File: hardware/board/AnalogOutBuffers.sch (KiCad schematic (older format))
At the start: 19 parts, among them U10 OPA4197

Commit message: Re-do the motherboard
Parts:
- added C15: 0.1uF, Capacitor_SMD:C_0603_1608Metric_Pad1.08x0.95mm_HandSolder, symbol Device:C_Small
- added R36: 1k, Resistor_SMD:R_0603_1608Metric_Pad0.98x0.95mm_HandSolder, symbol Device:R_US
- added U2: LM4040-10, Package_TO_SOT_SMD:SOT-23, symbol winterbloom:LM4040-10
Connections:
- net -12V: now also R36.1
- net GND: now also C15.1, U2.1 (K)
- net -10V renamed -10v_DAC
- net -10v_DAC: now also C15.2, R36.2, U2.2 (A)
- net DAC_IN_1 renamed DAC_1_PRE
- net DAC_IN_2 renamed DAC_2_PRE
- net DAC_IN_3 renamed DAC_3_PRE
- net DAC_IN_4 renamed DAC_4_PRE
- net DAC_OUT_1 renamed DAC_3_POST
- net DAC_OUT_2 renamed DAC_4_POST
- net DAC_OUT_3 renamed DAC_1_POST
- net DAC_OUT_4 renamed DAC_2_POST
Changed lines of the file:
@@
 $Descr A4 11693 8268
 encoding utf-8
-Sheet 5 7
-Title ""
-Date ""
-Rev ""
-Comp ""
-Comment1 ""
-Comment2 ""
+Sheet 4 7
+Title "TestKit Motherboard"
+Date "2021-10-22"
+Rev "v1"
+Comp "Winterbloom"
+Comment1 "Alethea Flowers"
+Comment2 "CERN-OHL-P V2"
 Comment3 ""
 Comment4 ""
@@
 Wire Wire Line
 	1625 1400 1675 1400
-$Comp
-L power:-10V #PWR068
-U 1 1 60917606
-P 1150 1950
-F 0 "#PWR068" H 1150 2050 50  0001 C CNN
-F 1 "-10V" V 1150 2175 50  0000 C CNN
-F 2 "" H 1150 1950 50  0001 C CNN
-F 3 "" H 1150 1950 50  0001 C CNN
-	1    1150 1950
-	0    -1   -1   0
-$EndComp
 Wire Wire Line
 	2575 1500 2575 1950
@@
 Wire Wire Line
 	1650 2400 1700 2400
-$Comp
-L power:-10V #PWR069
-U 1 1 60917658
-P 1175 2950
-F 0 "#PWR069" H 1175 3050 50  0001 C CNN
-F 1 "-10V" V 1175 3175 50  0000 C CNN
-F 2 "" H 1175 2950 50  0001 C CNN
-F 3 "" H 1175 2950 50  0001 C CNN
-	1    1175 2950
-	0    -1   -1   0
-$EndComp
 Wire Wire Line
 	2600 2500 2600 2950
@@
 Wire Wire Line
 	1650 3375 1700 3375
-$Comp
-L power:-10V #PWR070
-U 1 1 60917690
-P 1175 3925
-F 0 "#PWR070" H 1175 4025 50  0001 C CNN
-F 1 "-10V" V 1175 4150 50  0000 C CNN
-F 2 "" H 1175 3925 50  0001 C CNN
-F 3 "" H 1175 3925 50  0001 C CNN
-	1    1175 3925
-	0    -1   -1   0
-$EndComp
 Wire Wire Line
 	2600 3475 2600 3925
@@
 Wire Wire Line
 	1650 4350 1700 4350
-$Comp
-L power:-10V #PWR071
-U 1 1 609176C8
-P 1175 4900
-F 0 "#PWR071" H 1175 5000 50  0001 C CNN
-F 1 "-10V" V 1175 5125 50  0000 C CNN
-F 2 "" H 1175 4900 50  0001 C CNN
-F 3 "" H 1175 4900 50  0001 C CNN
-	1    1175 4900
-	0    -1   -1   0
-$EndComp
 Wire Wire Line
 	2600 4450 2600 4900
@@
 0 - 2.5v
 Text HLabel 1175 2600 0    50   Input ~ 0
-DAC_IN_2
+DAC_2_PRE
 Text HLabel 1175 3575 0    50   Input ~ 0
-DAC_IN_3
+DAC_3_PRE
 Text HLabel 2600 3475 2    50   Input ~ 0
-DAC_OUT_1
+DAC_3_POST
 Text HLabel 2600 4450 2    50   Input ~ 0
-DAC_OUT_2
+DAC_4_POST
 Text HLabel 2575 1500 2    50   Input ~ 0
-DAC_OUT_3
+DAC_1_POST
 Text HLabel 2600 2500 2    50   Input ~ 0
-DAC_OUT_4
+DAC_2_POST
 $Comp
 L winterbloom:OPA4197 U10
@@
 $EndComp
 Text HLabel 1175 4550 0    50   Input ~ 0
-DAC_IN_4
+DAC_4_PRE
 Text HLabel 1150 1600 0    50   Input ~ 0
-DAC_IN_1
+DAC_1_PRE
+$Comp
+L winterbloom:LM4040-10 U?
+U 1 1 617993BE
+P 5075 3375
+AR Path="/60711259/617993BE" Ref="U?"  Part="1"
+AR Path="/61059808/617993BE" Ref="U?"  Part="1"
+AR Path="/608FFE97/617993BE" Ref="U2"  Part="1"
+F 0 "U2" V 5029 3454 50  0000 L CNN
+F 1 "LM4040-10" V 5120 3454 50  0000 L CNN
+F 2 "Package_TO_SOT_SMD:SOT-23" H 5075 3175 50  0001 C CIN
+F 3 "http://www.ti.com/lit/ds/symlink/lm4040-n.pdf" H 5075 3375 50  0001 C CIN
+F 4 "LM4040DIM3-10.0/NOPB" H 5075 3575 50  0001 C CNN "mpn"
+	1    5075 3375
+	0    1    1    0
+$EndComp
+$Comp
+L Device:R_US R?
+U 1 1 617993C4
+P 5075 3075
+AR Path="/60711259/617993C4" Ref="R?"  Part="1"
+AR Path="/61059808/617993C4" Ref="R?"  Part="1"
+AR Path="/608FFE97/617993C4" Ref="R36"  Part="1"
+F 0 "R36" H 5143 3121 50  0000 L CNN
+F 1 "1k" H 5143 3030 50  0000 L CNN
+F 2 "Resistor_SMD:R_0603_1608Metric_Pad0.98x0.95mm_HandSolder" V 5115 3065 50  0001 C CNN
+F 3 "~" H 5075 3075 50  0001 C CNN
+	1    5075 3075
+	1    0    0    -1
+$EndComp
+$Comp
+L power:GND #PWR?
+U 1 1 617993CA
+P 5075 3525
+AR Path="/60711259/617993CA" Ref="#PWR?"  Part="1"
+AR Path="/61059808/617993CA" Ref="#PWR?"  Part="1"
+AR Path="/608FFE97/617993CA" Ref="#PWR0159"  Part="1"
+F 0 "#PWR0159" H 5075 3275 50  0001 C CNN
+F 1 "GND" H 5150 3375 50  0000 R CNN
+F 2 "" H 5075 3525 50  0001 C CNN
+F 3 "" H 5075 3525 50  0001 C CNN
+	1    5075 3525
+	1    0    0    -1
+$EndComp
+$Comp
+L power:-12V #PWR?
+U 1 1 617993D0
+P 5075 2925
+AR Path="/60711259/617993D0" Ref="#PWR?"  Part="1"
+AR Path="/61059808/617993D0" Ref="#PWR?"  Part="1"
+AR Path="/608FFE97/617993D0" Ref="#PWR0160"  Part="1"
+F 0 "#PWR0160" H 5075 3025 50  0001 C CNN
+F 1 "-12V" H 4975 3075 50  0000 L CNN
+F 2 "" H 5075 2925 50  0001 C CNN
+F 3 "" H 5075 2925 50  0001 C CNN
+	1    5075 2925
+	1    0    0    -1
+$EndComp
+$Comp
+L Device:C_Small C?
+U 1 1 617993D6
+P 4825 3375
+AR Path="/60711259/617993D6" Ref="C?"  Part="1"
+AR Path="/61059808/617993D6" Ref="C?"  Part="1"
+AR Path="/608FFE97/617993D6" Ref="C15"  Part="1"
+F 0 "C15" H 5000 3350 50  0000 R CNN
+F 1 "0.1uF" H 5125 3425 50  0000 R CNN
+F 2 "Capacitor_SMD:C_0603_1608Metric_Pad1.08x0.95mm_HandSolder" H 4825 3375 50  0001 C CNN
+F 3 "~" H 4825 3375 50  0001 C CNN
+	1    4825 3375
+	-1   0    0    1
+$EndComp
+Wire Wire Line
+	4825 3275 4825 3225
+Wire Wire Line
+	4825 3225 5075 3225
+Connection ~ 5075 3225
+Wire Wire Line
+	4825 3475 4825 3525
+Wire Wire Line
+	4825 3525 5075 3525
+Connection ~ 5075 3525
+Text Label 5275 3225 0    50   ~ 0
+-10v_DAC
+Wire Wire Line
+	5275 3225 5075 3225
+Text Label 1150 1950 2    50   ~ 0
+-10v_DAC
+Text Label 1175 2950 2    50   ~ 0
+-10v_DAC
+Text Label 1175 3925 2    50   ~ 0
+-10v_DAC
+Text Label 1175 4900 2    50   ~ 0
+-10v_DAC
 $EndSCHEMATC

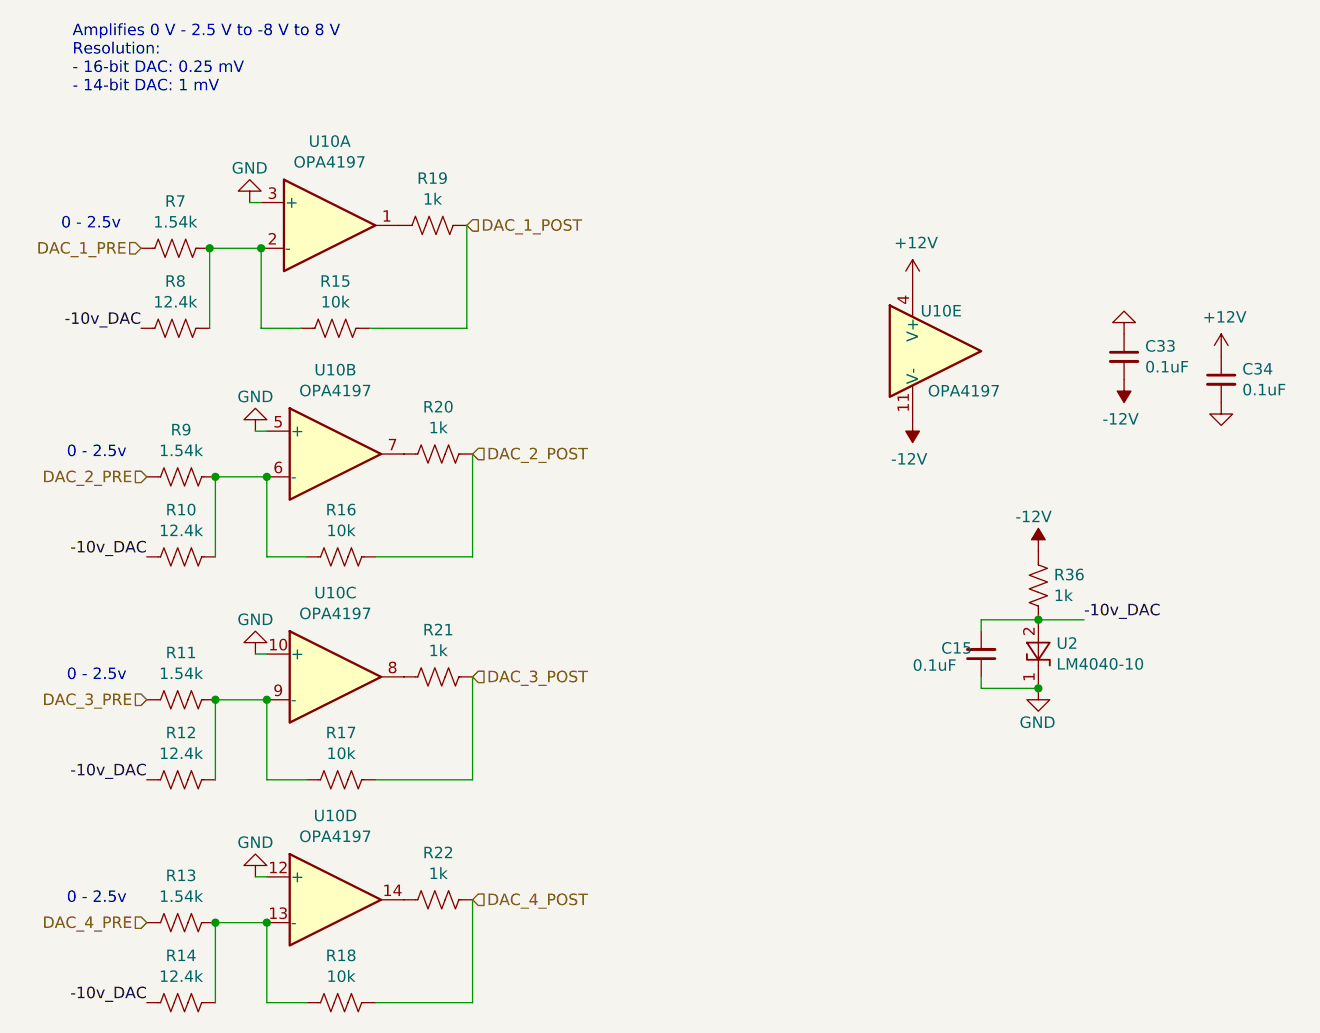
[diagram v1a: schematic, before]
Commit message: Fix issues found in hardware v1
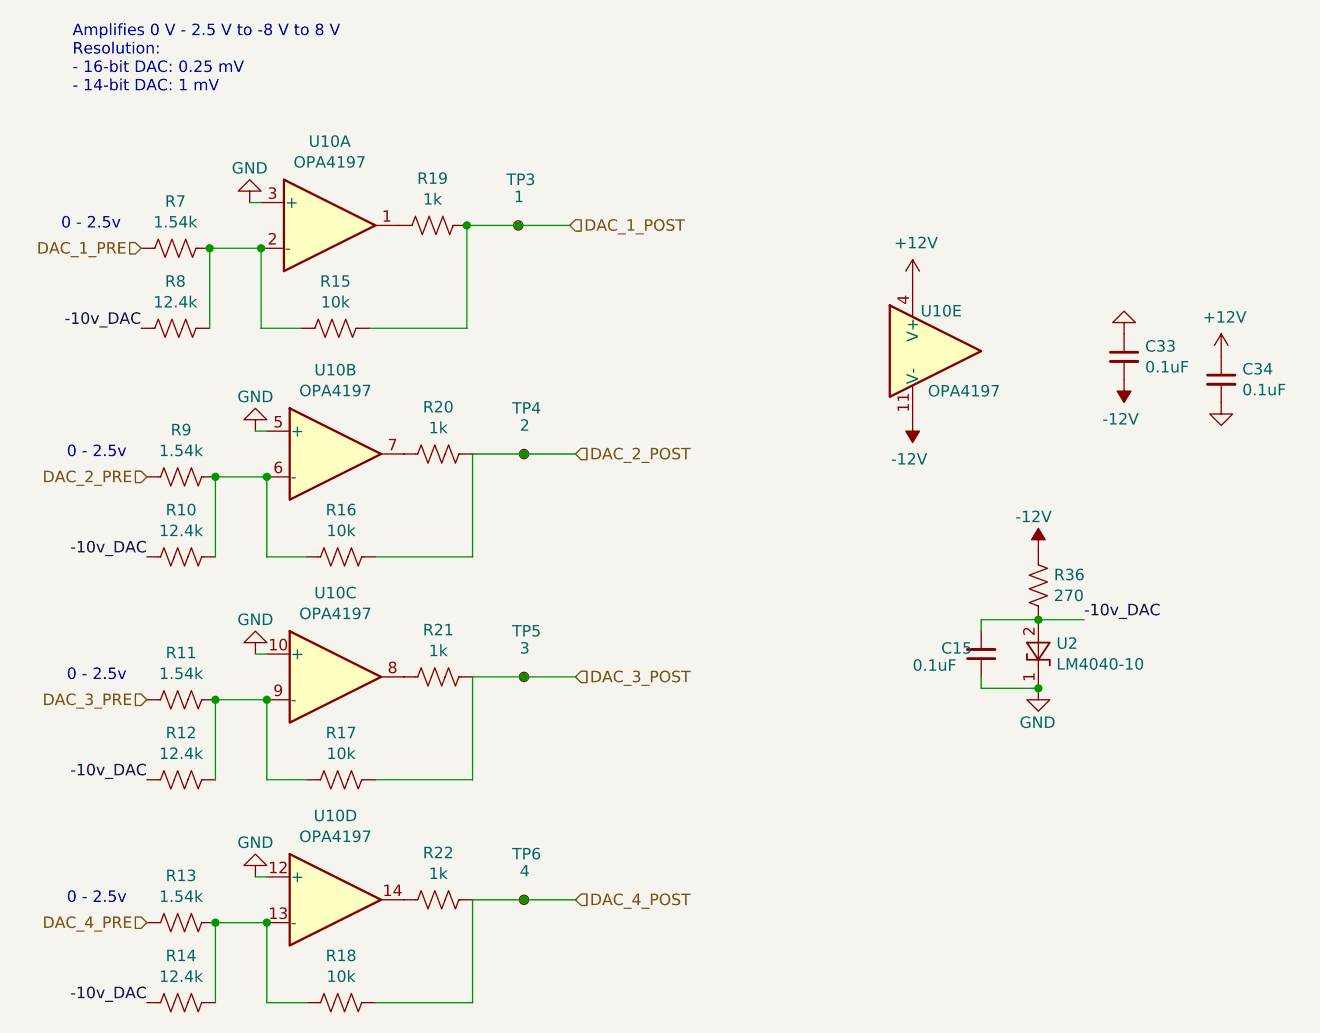
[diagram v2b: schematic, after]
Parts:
- added TP3: 1, TestPoint:TestPoint_Pad_D1.0mm, symbol Connector:TestPoint_Small
- added TP4: 2, TestPoint:TestPoint_Pad_D1.0mm, symbol Connector:TestPoint_Small
- added TP5: 3, TestPoint:TestPoint_Pad_D1.0mm, symbol Connector:TestPoint_Small
- added TP6: 4, TestPoint:TestPoint_Pad_D1.0mm, symbol Connector:TestPoint_Small
- R36: value 1k -> 270
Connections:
- net DAC_1_POST: now also TP3.1
- net DAC_2_POST: now also TP4.1
- net DAC_3_POST: now also TP5.1
- net DAC_4_POST: now also TP6.1
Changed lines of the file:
@@
 Sheet 4 7
 Title "TestKit Motherboard"
-Date "2021-10-22"
-Rev "v1"
+Date "2021-11-12"
+Rev "v2"
 Comp "Winterbloom"
 Comment1 "Alethea Flowers"
@@
 Text HLabel 1175 3575 0    50   Input ~ 0
 DAC_3_PRE
-Text HLabel 2600 3475 2    50   Input ~ 0
+Text HLabel 3050 3475 2    50   Input ~ 0
 DAC_3_POST
-Text HLabel 2600 4450 2    50   Input ~ 0
+Text HLabel 3050 4450 2    50   Input ~ 0
 DAC_4_POST
-Text HLabel 2575 1500 2    50   Input ~ 0
+Text HLabel 3025 1500 2    50   Input ~ 0
 DAC_1_POST
-Text HLabel 2600 2500 2    50   Input ~ 0
+Text HLabel 3050 2500 2    50   Input ~ 0
 DAC_2_POST
 $Comp
@@
 AR Path="/608FFE97/617993C4" Ref="R36"  Part="1"
 F 0 "R36" H 5143 3121 50  0000 L CNN
-F 1 "1k" H 5143 3030 50  0000 L CNN
+F 1 "270" H 5143 3030 50  0000 L CNN
 F 2 "Resistor_SMD:R_0603_1608Metric_Pad0.98x0.95mm_HandSolder" V 5115 3065 50  0001 C CNN
 F 3 "~" H 5075 3075 50  0001 C CNN
@@
 Text Label 1175 4900 2    50   ~ 0
 -10v_DAC
+$Comp
+L Connector:TestPoint_Small TP?
+U 1 1 618195C6
+P 2800 1500
+AR Path="/617FCAA5/618195C6" Ref="TP?"  Part="1"
+AR Path="/608FFE97/618195C6" Ref="TP3"  Part="1"
+F 0 "TP3" V 2600 1575 50  0000 R CNN
+F 1 "1" V 2675 1525 50  0000 R CNN
+F 2 "TestPoint:TestPoint_Pad_D1.0mm" H 3000 1500 50  0001 C CNN
+F 3 "~" H 3000 1500 50  0001 C CNN
+	1    2800 1500
+	0    1    1    0
+$EndComp
+Wire Wire Line
+	2575 1500 2800 1500
+Connection ~ 2575 1500
+Wire Wire Line
+	2800 1500 3025 1500
+Connection ~ 2800 1500
+$Comp
+L Connector:TestPoint_Small TP?
+U 1 1 6181CE72
+P 2825 2500
+AR Path="/617FCAA5/6181CE72" Ref="TP?"  Part="1"
+AR Path="/608FFE97/6181CE72" Ref="TP4"  Part="1"
+F 0 "TP4" V 2625 2575 50  0000 R CNN
+F 1 "2" V 2700 2525 50  0000 R CNN
+F 2 "TestPoint:TestPoint_Pad_D1.0mm" H 3025 2500 50  0001 C CNN
+F 3 "~" H 3025 2500 50  0001 C CNN
+	1    2825 2500
+	0    1    1    0
+$EndComp
+Wire Wire Line
+	2600 2500 2825 2500
+Wire Wire Line
+	2825 2500 3050 2500
+Connection ~ 2825 2500
+$Comp
+L Connector:TestPoint_Small TP?
+U 1 1 6181D989
+P 2825 3475
+AR Path="/617FCAA5/6181D989" Ref="TP?"  Part="1"
+AR Path="/608FFE97/6181D989" Ref="TP5"  Part="1"
+F 0 "TP5" V 2625 3550 50  0000 R CNN
+F 1 "3" V 2700 3500 50  0000 R CNN
+F 2 "TestPoint:TestPoint_Pad_D1.0mm" H 3025 3475 50  0001 C CNN
+F 3 "~" H 3025 3475 50  0001 C CNN
+	1    2825 3475
+	0    1    1    0
+$EndComp
+Wire Wire Line
+	2600 3475 2825 3475
+Wire Wire Line
+	2825 3475 3050 3475
+Connection ~ 2825 3475
+$Comp
+L Connector:TestPoint_Small TP?
+U 1 1 6181E6EB
+P 2825 4450
+AR Path="/617FCAA5/6181E6EB" Ref="TP?"  Part="1"
+AR Path="/608FFE97/6181E6EB" Ref="TP6"  Part="1"
+F 0 "TP6" V 2625 4525 50  0000 R CNN
+F 1 "4" V 2700 4475 50  0000 R CNN
+F 2 "TestPoint:TestPoint_Pad_D1.0mm" H 3025 4450 50  0001 C CNN
+F 3 "~" H 3025 4450 50  0001 C CNN
+	1    2825 4450
+	0    1    1    0
+$EndComp
+Wire Wire Line
+	2600 4450 2825 4450
+Wire Wire Line
+	2825 4450 3050 4450
+Connection ~ 2825 4450
 $EndSCHEMATC
